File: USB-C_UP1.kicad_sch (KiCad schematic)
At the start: 23 parts, among them J12 USB_C_Receptacle, J13 I2C_HD3SS3220, U1 HD3SS3220IRNHR, U22 TPD4E02B04DQA, U23 TPD4E02B04DQA, U24 TPD4E02B04DQA

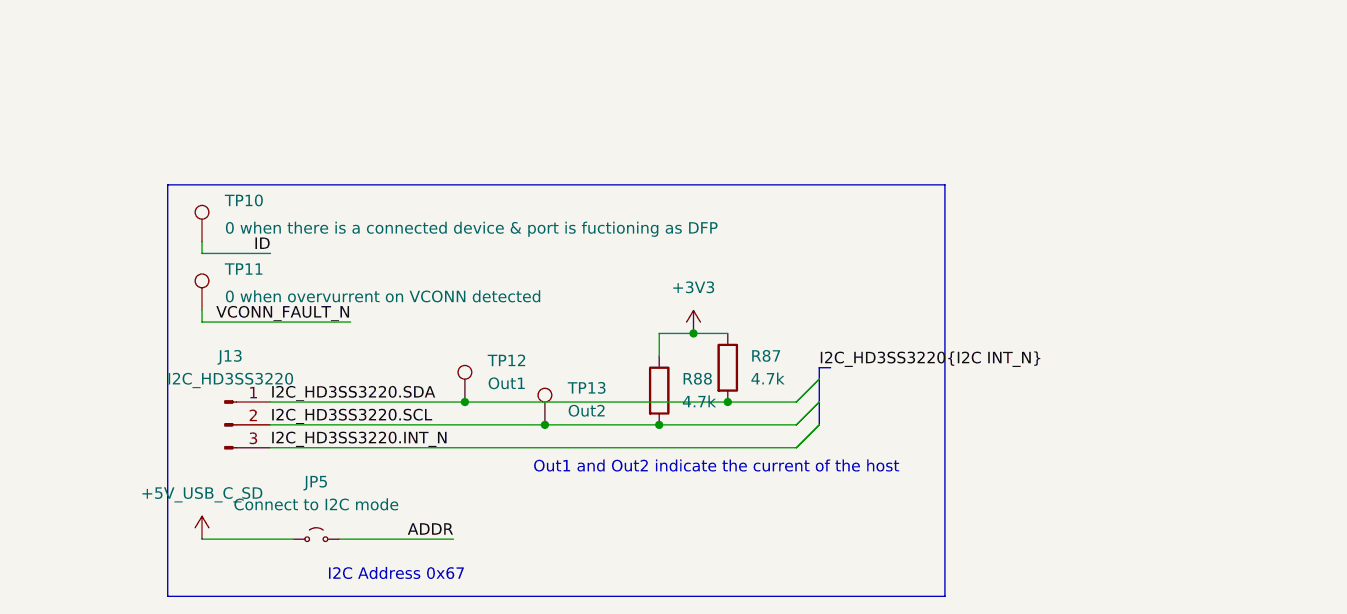
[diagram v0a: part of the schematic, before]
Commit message: Ferrite bread filter for LDO and MIC23201, labelling improved
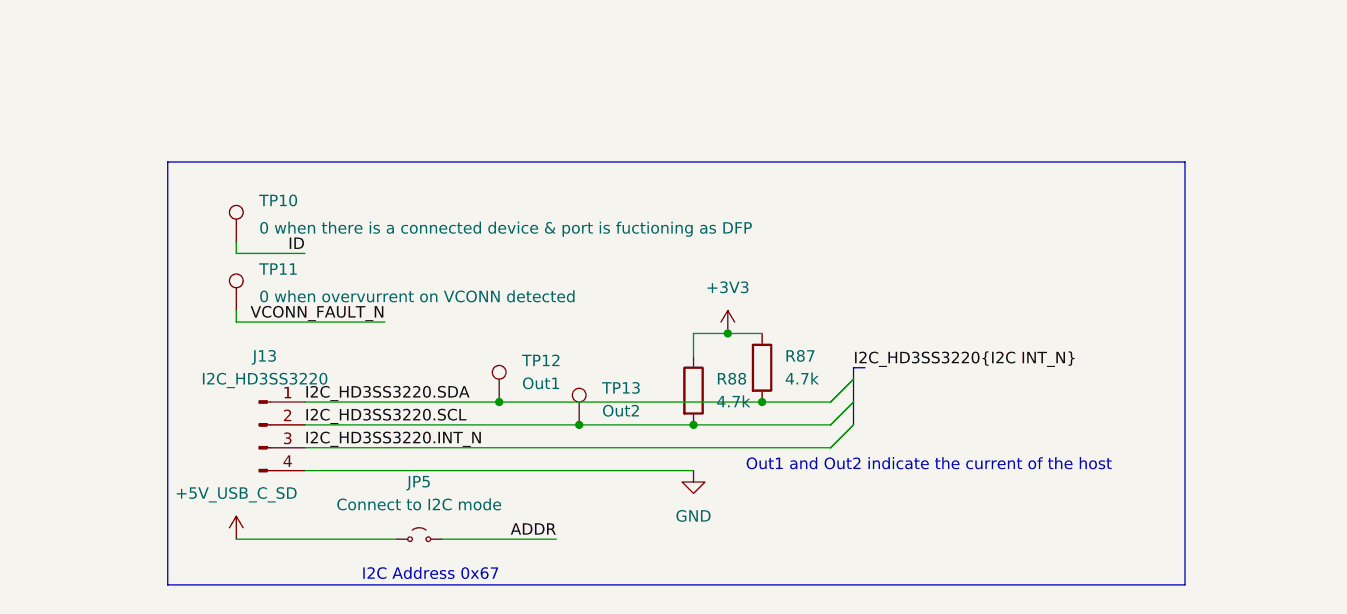
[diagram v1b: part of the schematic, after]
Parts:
- J13: symbol Connector:Conn_01x03_Pin -> Connector:Conn_01x04_Pin
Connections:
- net GND: now also J13.4 (Pin_4)
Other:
- moved on the sheet: JP5, R87, R88, TP10, TP11, TP12, TP13

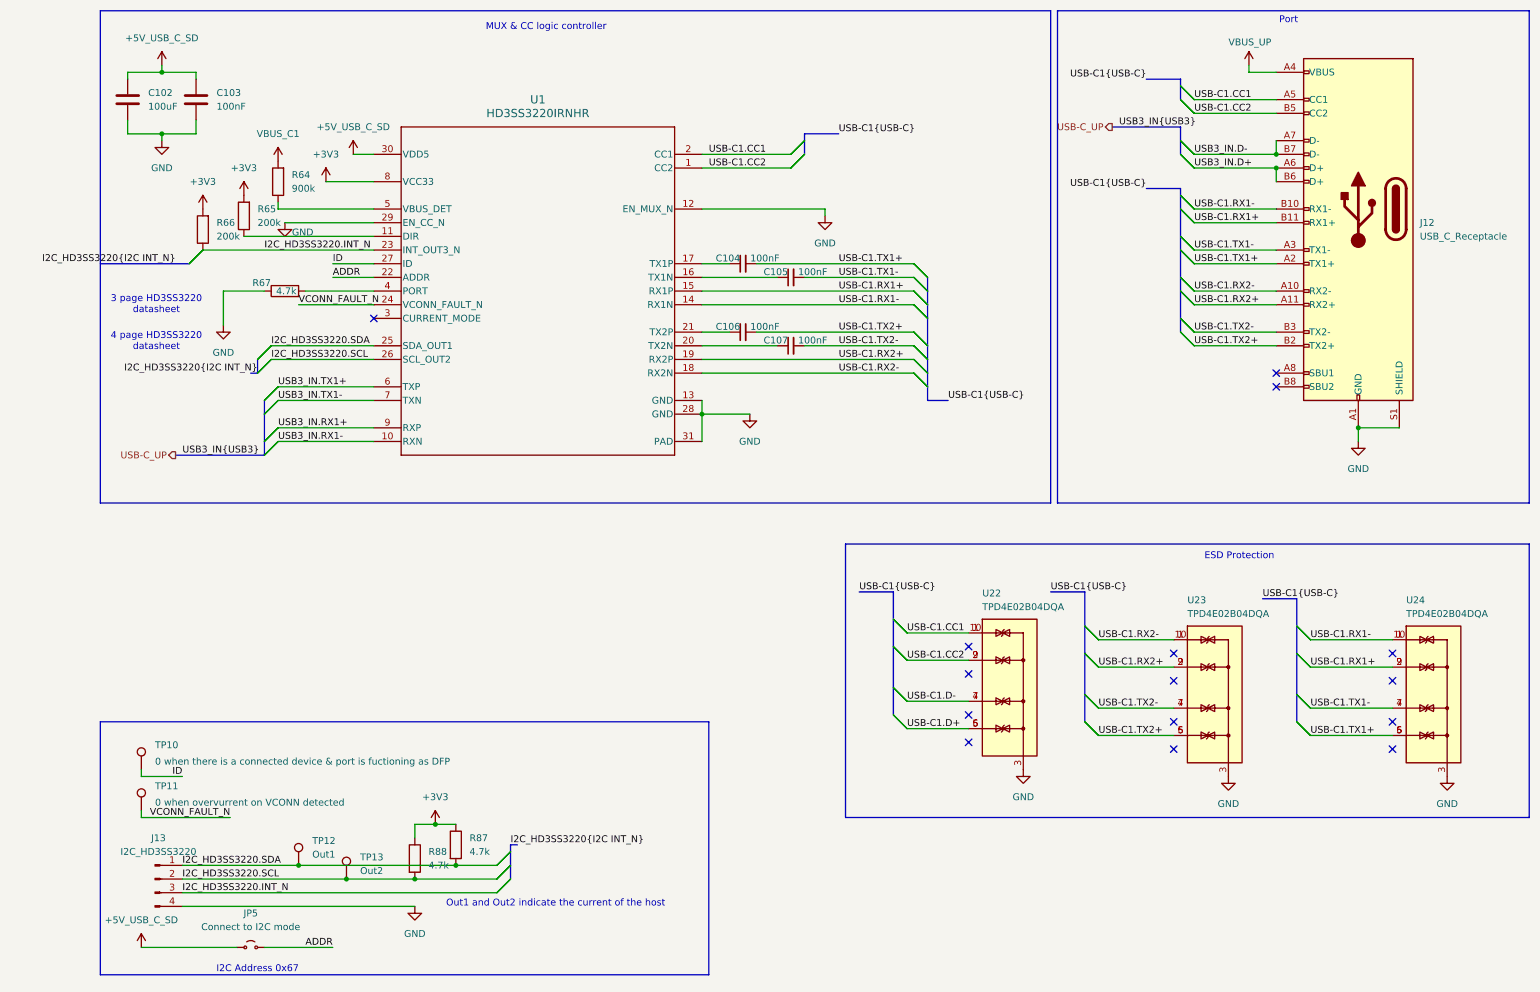
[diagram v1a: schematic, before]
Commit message: Schematic reannotated
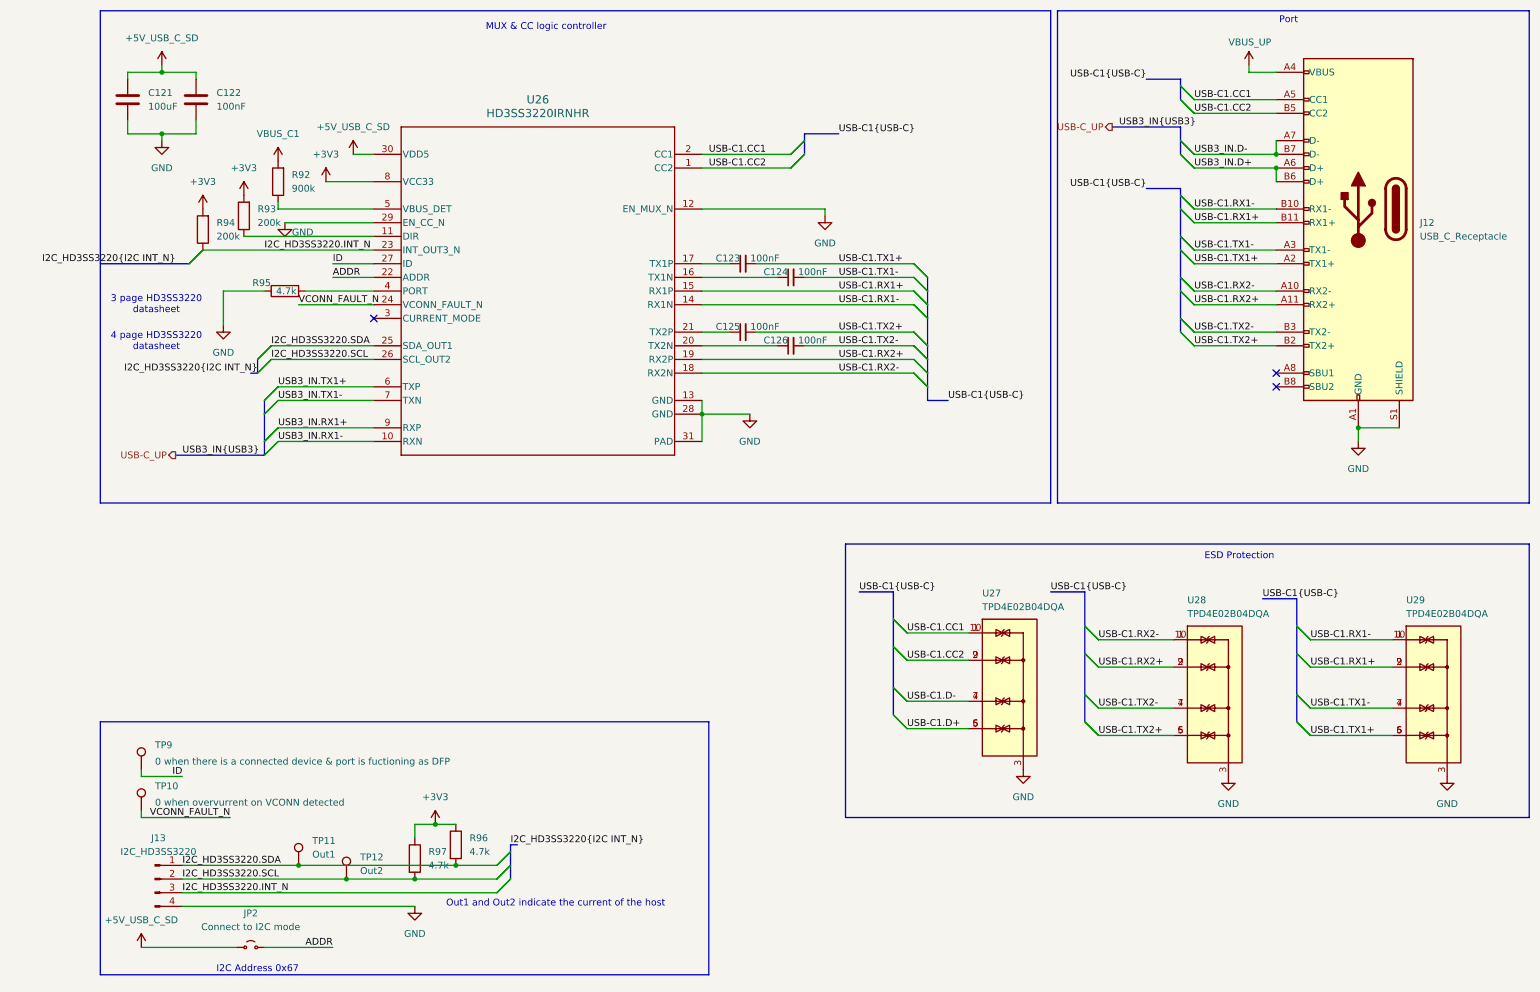
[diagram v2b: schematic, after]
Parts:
- renumbered C102 to C121, C103 to C122, C104 to C123, C105 to C124, C106 to C125, C107 to C126, JP5 to JP2, R64 to R92, R65 to R93, R66 to R94, R67 to R95, R87 to R96, R88 to R97, TP11 to TP10, TP12 to TP11, TP13 to TP12, TP10 to TP9, U1 to U26, U22 to U27, U23 to U28, U24 to U29
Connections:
- no-connect marks 15 -> 3

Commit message: J11 changed to 8-pin PCIe connector, footprint assigned
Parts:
- R96, R97: footprint (none) -> Resistor_SMD:R_0402_1005Metric
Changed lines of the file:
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@@
 			)
 		)
-		(property "Footprint" ""
+		(property "Footprint" "Resistor_SMD:R_0402_1005Metric"
 			(at 79.502 168.91 90)
 			(effects
@@
 			)
 		)
-		(property "Footprint" ""
+		(property "Footprint" "Resistor_SMD:R_0402_1005Metric"
 			(at 71.882 171.45 90)
 			(effects

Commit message: footprints assigned, U21 change to SiRA80DP
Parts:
- TP10, TP11, TP12, TP9: footprint TestPoint:TestPoint_2Pads_Pitch5.08mm_Drill1.3mm -> TestPoint:TestPoint_Loop_D1.80mm_Drill1.0mm_Beaded
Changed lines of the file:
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@@
 			)
 		)
-		(property "Footprint" "TestPoint:TestPoint_2Pads_Pitch5.08mm_Drill1.3mm"
+		(property "Footprint" "TestPoint:TestPoint_Loop_D1.80mm_Drill1.0mm_Beaded"
 			(at 57.15 172.72 0)
 			(effects
@@
 			)
 		)
-		(property "Footprint" "TestPoint:TestPoint_2Pads_Pitch5.08mm_Drill1.3mm"
+		(property "Footprint" "TestPoint:TestPoint_Loop_D1.80mm_Drill1.0mm_Beaded"
 			(at 66.04 175.26 0)
 			(effects
@@
 			)
 		)
-		(property "Footprint" "TestPoint:TestPoint_2Pads_Pitch5.08mm_Drill1.3mm"
+		(property "Footprint" "TestPoint:TestPoint_Loop_D1.80mm_Drill1.0mm_Beaded"
 			(at 27.94 162.56 0)
 			(effects
@@
 			)
 		)
-		(property "Footprint" "TestPoint:TestPoint_2Pads_Pitch5.08mm_Drill1.3mm"
+		(property "Footprint" "TestPoint:TestPoint_Loop_D1.80mm_Drill1.0mm_Beaded"
 			(at 27.94 154.94 0)
 			(effects

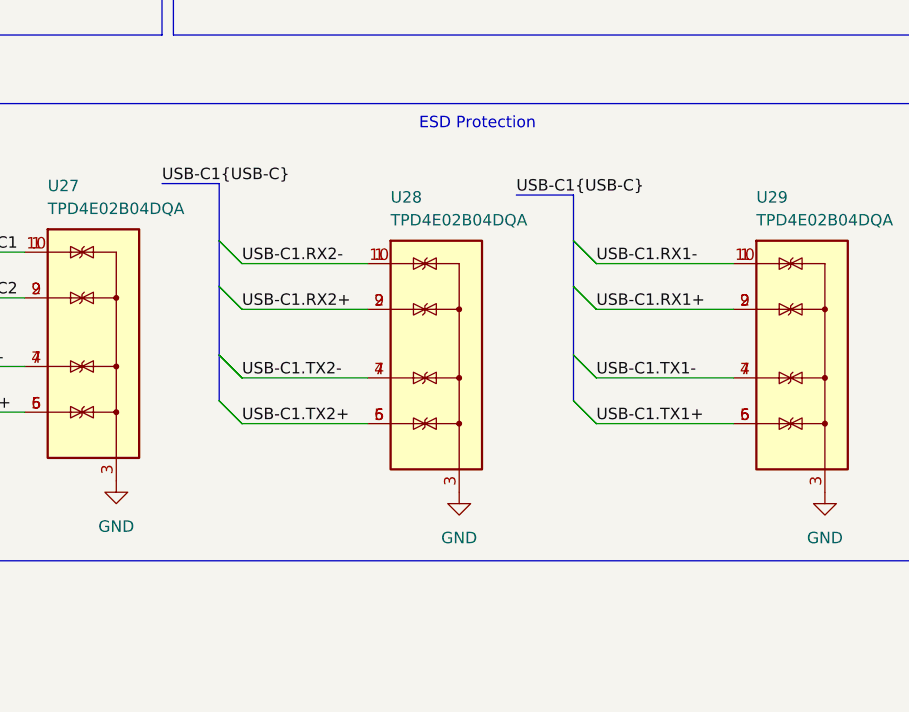
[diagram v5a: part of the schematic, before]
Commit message: Next net class label fixes, swap of the SS lines for better routing
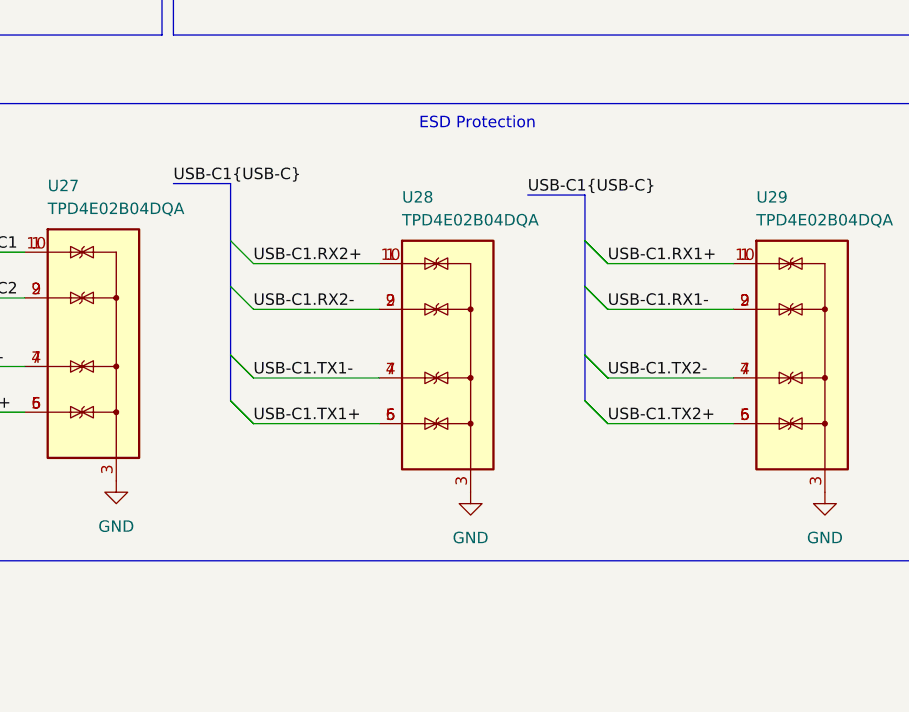
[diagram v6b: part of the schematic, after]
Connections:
- net USB-C1.RX1+: now also U29.1 (IO1), U29.10 (NC); no longer U29.2 (IO2), U29.9 (NC)
- net USB-C1.RX1-: now also U29.2 (IO2), U29.9 (NC); no longer U29.1 (IO1), U29.10 (NC)
- net USB-C1.RX2+: now also U28.1 (IO1), U28.10 (NC); no longer U28.2 (IO2), U28.9 (NC)
- net USB-C1.RX2-: now also U28.2 (IO2), U28.9 (NC); no longer U28.1 (IO1), U28.10 (NC)
- net USB-C1.TX1+: now also U28.5 (IO4), U28.6 (NC); no longer U29.5 (IO4), U29.6 (NC)
- net USB-C1.TX1-: now also U28.4 (IO3), U28.7 (NC); no longer U29.4 (IO3), U29.7 (NC)
- net USB-C1.TX2+: now also U29.5 (IO4), U29.6 (NC); no longer U28.5 (IO4), U28.6 (NC)
- net USB-C1.TX2-: now also U29.4 (IO3), U29.7 (NC); no longer U28.4 (IO3), U28.7 (NC)

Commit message: scheme regenerated
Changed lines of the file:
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@@
 	(bus
 		(pts
-			(xy 203.2 35.56) (xy 215.9 35.56)
+			(xy 204.47 35.56) (xy 215.9 35.56)
 		)
 		(stroke
@@
 	(hierarchical_label "USB-C_UP"
 		(shape output)
-		(at 203.2 35.56 180)
-		(effects
-			(font
+		(at 204.47 35.56 180)
+		(effects
+			(font

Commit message: Added lcsc part number for most of components, fixes for better routing
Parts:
- C121: footprint Capacitor_THT:C_Radial_D10.0mm_H16.0mm_P5.00mm -> Capacitor_THT:C_Radial_D6.3mm_H11.0mm_P2.50mm; LCSC Part (none) -> C109392
- C122, C123, C124, C125, C126: LCSC Part (none) -> C5182432
- U26: LCSC Part (none) -> C165155
- U27, U28, U29: LCSC Part (none) -> C106794
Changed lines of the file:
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@@
+			)
+		)
+		(property "LCSC Part" "C165155"
+			(at 96.52 66.04 0)
+			(effects
+				(font
+					(size 1.27 1.27)
+				)
+				(hide yes)
 			)
 		)
@@
 			)
 		)
+		(property "LCSC Part" "C5182432"
+			(at 134.62 73.66 90)
+			(effects
+				(font
+					(size 1.27 1.27)
+				)
+				(hide yes)
+			)
+		)
 		(pin "2"
 		)
@@
 			)
 		)
+		(property "LCSC Part" "C106794"
+			(at 223.52 140.97 0)
+			(effects
+				(font
+					(size 1.27 1.27)
+				)
+				(hide yes)
+			)
+		)
 		(pin "5"
 		)
@@
 			)
 		)
+		(property "LCSC Part" "C106794"
+			(at 262.89 140.97 0)
+			(effects
+				(font
+					(size 1.27 1.27)
+				)
+				(hide yes)
+			)
+		)
 		(pin "5"
 		)
@@
 			)
 		)
+		(property "LCSC Part" "C5182432"
+			(at 134.62 60.96 90)
+			(effects
+				(font
+					(size 1.27 1.27)
+				)
+				(hide yes)
+			)
+		)
 		(pin "2"
 		)
@@
 			)
 		)
+		(property "LCSC Part" "C5182432"
+			(at 143.51 63.5 90)
+			(effects
+				(font
+					(size 1.27 1.27)
+				)
+				(hide yes)
+			)
+		)
 		(pin "2"
 		)
@@
 			)
 		)
+		(property "LCSC Part" "C5182432"
+			(at 143.51 76.2 90)
+			(effects
+				(font
+					(size 1.27 1.27)
+				)
+				(hide yes)
+			)
+		)
 		(pin "2"
 		)
@@
 			)
 		)
+		(property "LCSC Part" "C5182432"
+			(at 33.02 30.48 0)
+			(effects
+				(font
+					(size 1.27 1.27)
+				)
+				(hide yes)
+			)
+		)
 		(pin "2"
 		)
@@
 			)
 		)
+		(property "LCSC Part" "C106794"
+			(at 184.15 139.7 0)
+			(effects
+				(font
+					(size 1.27 1.27)
+				)
+				(hide yes)
+			)
+		)
 		(pin "5"
 		)
@@
 			)
 		)
-		(property "Footprint" "Capacitor_THT:C_Radial_D10.0mm_H16.0mm_P5.00mm"
+		(property "Footprint" "Capacitor_THT:C_Radial_D6.3mm_H11.0mm_P2.50mm"
 			(at 21.2852 34.29 0)
 			(effects
@@
 			(at 20.32 30.48 0)
 			(effects
+				(font
+					(size 1.27 1.27)
+				)
+				(hide yes)
+			)
+		)
+		(property "LCSC Part" "C109392"
+			(at 20.32 30.48 0)
+			(effects
